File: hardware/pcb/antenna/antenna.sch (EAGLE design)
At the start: 25 parts, among them Q2 2N3819, T1 2N5089, X2 SMA-142-0701-801/806

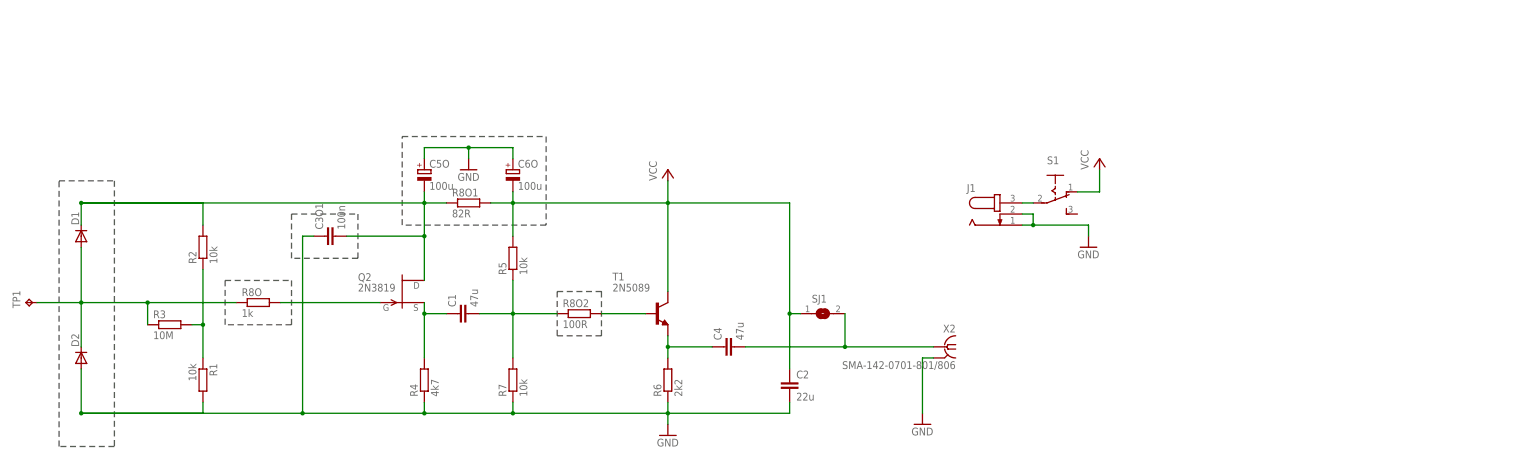
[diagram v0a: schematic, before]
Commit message: hw: added libs, modified receiver doc: added "proces dyplomowania" doc: added sample tex documents
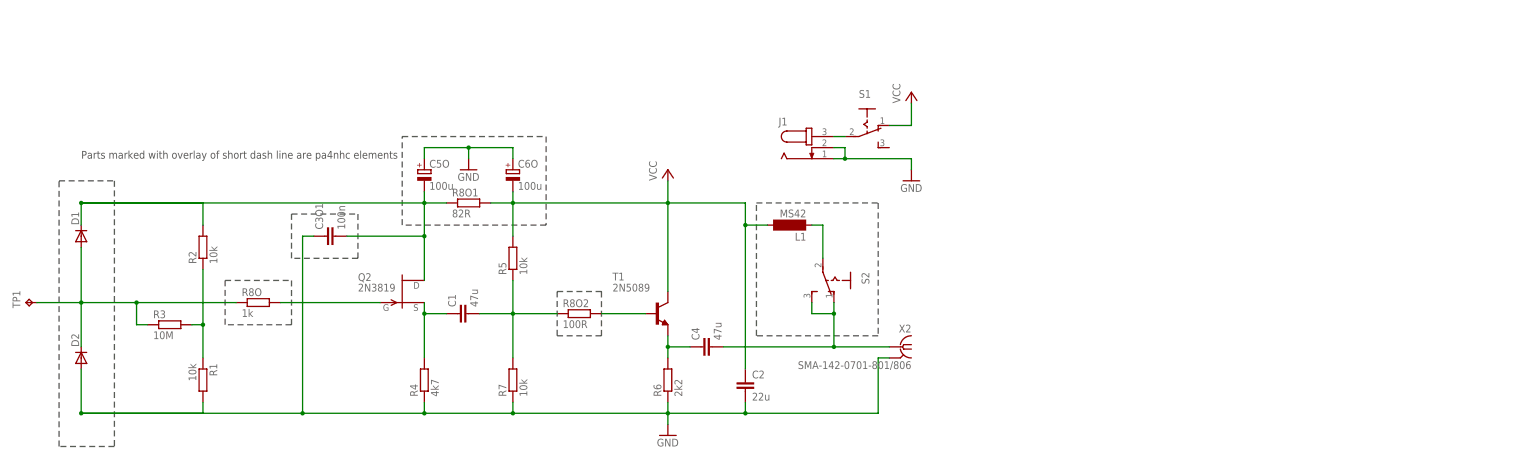
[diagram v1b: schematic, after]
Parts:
- removed SJ1: (no value), jumper:SJW
- added L1: MS42, inductor-neosid:MS42
- added S2: (no value), switch:255SB
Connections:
- new net N$6: L1.1, S2.P
- net N$7: now also S2.O, S2.S; no longer SJ1.2
- net VCC: now also L1.2; no longer SJ1.1
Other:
- note added: "Parts marked with overlay of short dash line are pa4nhc elements"
- moved on the sheet: C2, C4, J1, S1, X2

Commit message: hw: misc changes, added fuses to power supply units
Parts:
- added F1: 200mA, fuse:GSH15
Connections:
- new net N$12: F1.1, S1.O
- net VCC: now also F1.2; no longer S1.O
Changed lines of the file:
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@@
 <setting verticaltext="up"/>
 </settings>
-<grid distance="0.1" unitdist="inch" unit="inch" style="lines" multiple="1" display="yes" altdistance="0.01" altunitdist="inch" altunit="inch"/>
+<grid distance="0.1" unitdist="inch" unit="inch" style="lines" multiple="1" display="no" altdistance="0.01" altunitdist="inch" altunit="inch"/>
 <layers>
 <layer number="1" name="Top" color="4" fill="1" visible="no" active="no"/>
@@
 <part name="S2" library="switch" deviceset="255SB" device=""/>
 <part name="L1" library="inductor-neosid" deviceset="MS42" device=""/>
+<part name="F1" library="fuse" deviceset="GSH15" device="" value="200mA"/>
 </parts>
 <sheets>
@@
 <instance part="C6O" gate="G$1" x="71.12" y="63.5"/>
 <instance part="GND1" gate="1" x="106.68" y="2.54"/>
-<instance part="GND2" gate="1" x="162.56" y="60.96"/>
+<instance part="GND2" gate="1" x="172.72" y="60.96"/>
 <instance part="GND3" gate="1" x="60.96" y="63.5"/>
 <instance part="TP1" gate="G$1" x="-40.64" y="33.02" rot="R90"/>
@@
 <instance part="X2" gate="G1" x="160.02" y="22.86" rot="MR0"/>
 <instance part="J1" gate="G$1" x="139.7" y="68.58"/>
-<instance part="P+1" gate="VCC" x="162.56" y="81.28"/>
+<instance part="P+1" gate="VCC" x="172.72" y="83.82"/>
 <instance part="S1" gate="1" x="152.4" y="73.66" rot="R270"/>
 <instance part="P+2" gate="VCC" x="106.68" y="63.5"/>
@@
 <instance part="S2" gate="1" x="144.78" y="38.1" rot="R180"/>
 <instance part="L1" gate="G$1" x="134.62" y="50.8" rot="R180"/>
+<instance part="F1" gate="1" x="165.1" y="73.66"/>
 </instances>
 <busses>
@@
 <pinref part="GND2" gate="1" pin="GND"/>
 <pinref part="J1" gate="G$1" pin="1"/>
-<wire x1="162.56" y1="66.04" x2="162.56" y2="63.5" width="0.1524" layer="91"/>
+<wire x1="172.72" y1="66.04" x2="172.72" y2="63.5" width="0.1524" layer="91"/>
 <wire x1="144.78" y1="66.04" x2="147.32" y2="66.04" width="0.1524" layer="91"/>
 <pinref part="J1" gate="G$1" pin="2"/>
-<wire x1="147.32" y1="66.04" x2="162.56" y2="66.04" width="0.1524" layer="91"/>
+<wire x1="147.32" y1="66.04" x2="172.72" y2="66.04" width="0.1524" layer="91"/>
 <wire x1="144.78" y1="68.58" x2="147.32" y2="68.58" width="0.1524" layer="91"/>
 <wire x1="147.32" y1="68.58" x2="147.32" y2="66.04" width="0.1524" layer="91"/>
@@
 <net name="VCC" class="0">
 <segment>
-<pinref part="S1" gate="1" pin="O"/>
-<wire x1="157.48" y1="73.66" x2="162.56" y2="73.66" width="0.1524" layer="91"/>
-<wire x1="162.56" y1="73.66" x2="162.56" y2="78.74" width="0.1524" layer="91"/>
-<pinref part="P+1" gate="VCC" pin="VCC"/>
-</segment>
-<segment>
 <pinref part="R5" gate="G$1" pin="2"/>
 <wire x1="71.12" y1="55.88" x2="106.68" y2="55.88" width="0.1524" layer="91"/>
@@
 <junction x="124.46" y="50.8"/>
 </segment>
+<segment>
+<pinref part="F1" gate="1" pin="2"/>
+<wire x1="170.18" y1="73.66" x2="172.72" y2="73.66" width="0.1524" layer="91"/>
+<wire x1="172.72" y1="73.66" x2="172.72" y2="81.28" width="0.1524" layer="91"/>
+<pinref part="P+1" gate="VCC" pin="VCC"/>
+</segment>
 </net>
 <net name="N$4" class="0">
@@
 </segment>
 </net>
+<net name="N$12" class="0">
+<segment>
+<pinref part="S1" gate="1" pin="O"/>
+<pinref part="F1" gate="1" pin="1"/>
+<wire x1="160.02" y1="73.66" x2="157.48" y2="73.66" width="0.1524" layer="91"/>
+</segment>
+</net>

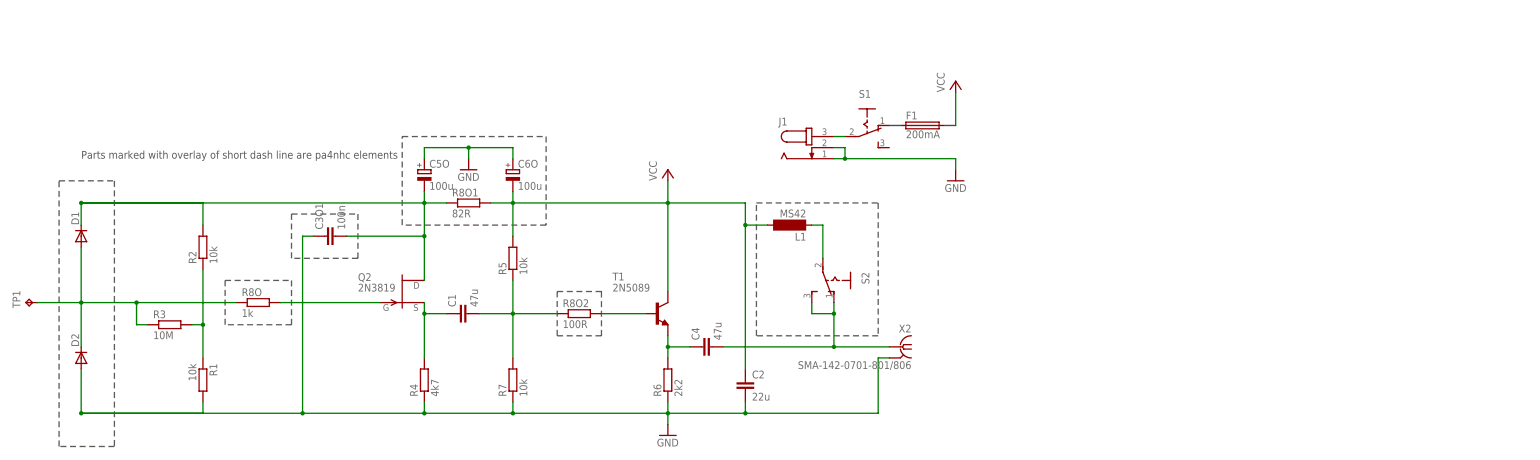
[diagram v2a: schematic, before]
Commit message: hw: added bibliography, fitler for 55MHz cutoff
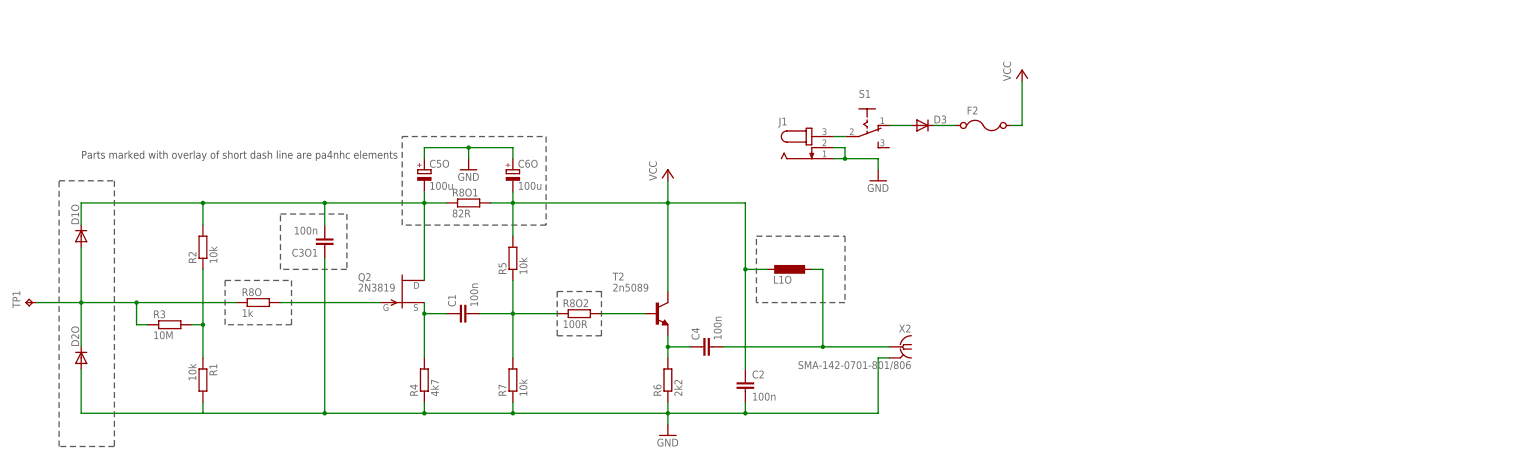
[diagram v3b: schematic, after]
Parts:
- removed D1, D2: (no value), diode:DIODE-SOD80C
- removed F1: 200mA, fuse:GSH15
- removed L1: MS42, inductor-neosid:MS42
- removed S2: (no value), switch:255SB
- removed T1: 2N5089, transistor:2N5089
- added D1O, D2O, D3: (no value), diode:DIODE-DO214AC
- added F2: (no value), lstolcman_thesis:0ZCG0150BF2C
- added L1O: (no value), rcl:L-EU0207/5V
- added T2: 2n5089, transistor:-NPN-SOT23-EBC
- C1, C4: value 47u -> 100n; MFR (none) -> C0805C104K5RACTU
- C2: value 22u -> 100n; MFR (none) -> C0805C104K5RACTU
- C3O1: MFR (none) -> C0805C104K5RACTU
- C5O, C6O: device rcl:CPOL-EUA/3216-18W -> rcl:CPOL-EUE2.5-7; MFR (none) -> 107CKS035M
- J1: MFR (none) -> 163-179PH-EX
- Q2: MFR (none) -> 2N3819 or 2N4859
- R1, R2, R5, R7: MFR (none) -> AS08J1002ET
- R3: MFR (none) -> SG73S2ATTD106J
- R4: MFR (none) -> SG73S2ATTD472J
- R6: device rcl:R-EU_M0805 -> rcl:R-EU_R2010; MFR (none) -> SG73P2ATTD222J
- R8O: MFR (none) -> AS08J1001ET
- R8O1: MFR (none) -> SG73S2ATTD820J
- R8O2: device rcl:R-EU_M0805 -> rcl:R-EU_M1206; MFR (none) -> AS08J1000ET
- S1: MFR (none) -> GF-123-3011
- TP1: MFR (none) -> LHL08TB100K
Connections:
- removed net N$7: C4.2, S2.O, S2.S, X2.1
- new net N$14: D3.C, F2.1
- net GND: now also D2O.A; no longer D2.A
- net N$1: now also D1O.A, D2O.C; no longer D1.A, D2.C
- net N$10: now also T2.B; no longer T1.B
- net N$12: now also D3.A; no longer F1.1
- net N$5: now also T2.E; no longer T1.E
- net N$6: now also C4.2, L1O.1, X2.1; no longer L1.1, S2.P
- net N$9: now also D1O.C; no longer D1.C
- net VCC: now also F2.2, L1O.2, T2.C; no longer F1.2, L1.2, T1.C
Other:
- moved on the sheet: C3O1

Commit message: hw: minor changes
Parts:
- added C3, C5, C6: 100n, rcl:C-EUC0805
- added L11: (no value), rcl:L-EU0207/5V
- added X1, X3: B35N57, con-coax:B35N57
- F2: MFR2 (none) -> 0ZCJ0020FF2E
- J1: MFR 163-179PH-EX -> FC68148; SUP (none) -> tme
- S1: MFR GF-123-3011 -> S1501; SUP (none) -> tme
- X2: value SMA-142-0701-801/806 -> B35N57; device con-coax:SMA-142-0701-801/806 -> con-coax:B35N57
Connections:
- new net N$13: D3.C, F2.2
- new net N$15: C6.1, X2.1
- new net N$7: C6.2, L11.2, X3.1
- net GND: now also C3.1, C5.1, X1.2, X3.2
- net N$12: now also C3.2, F2.1, L11.1; no longer D3.A, S1.O
- net N$14: now also C5.2, D3.A, S1.P; no longer D3.C, F2.1
- net N$6: now also X1.1; no longer X2.1
- net N$8: now also S1.O; no longer S1.P
- net VCC: no longer F2.2
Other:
- moved on the sheet: D3, F2, J1, S1

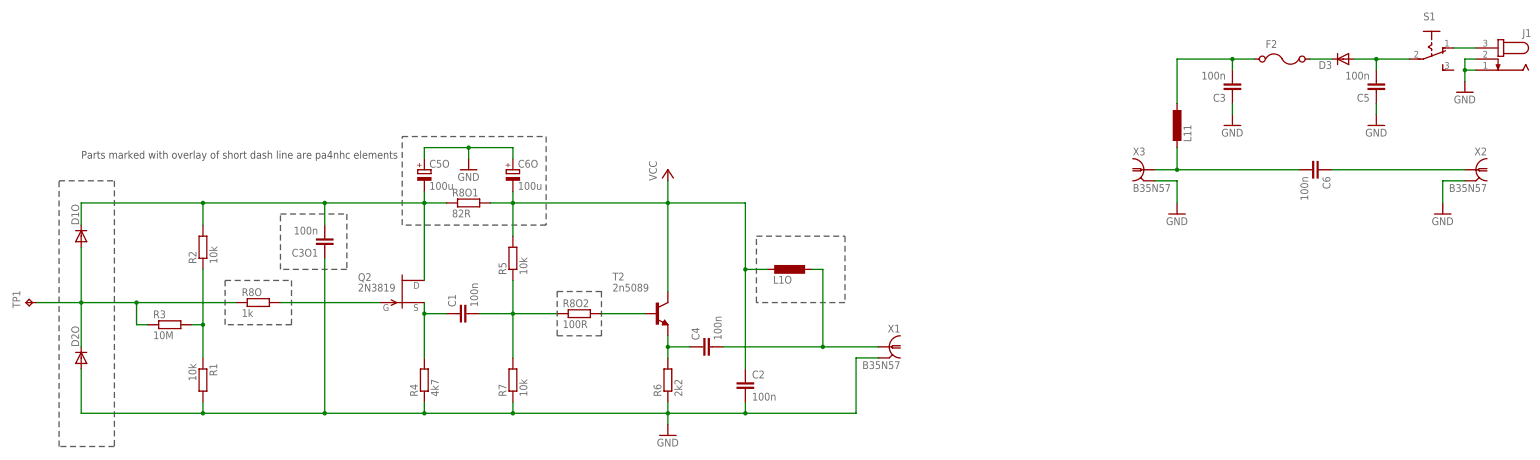
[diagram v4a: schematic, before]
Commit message: hw: bnc connector, misc changes
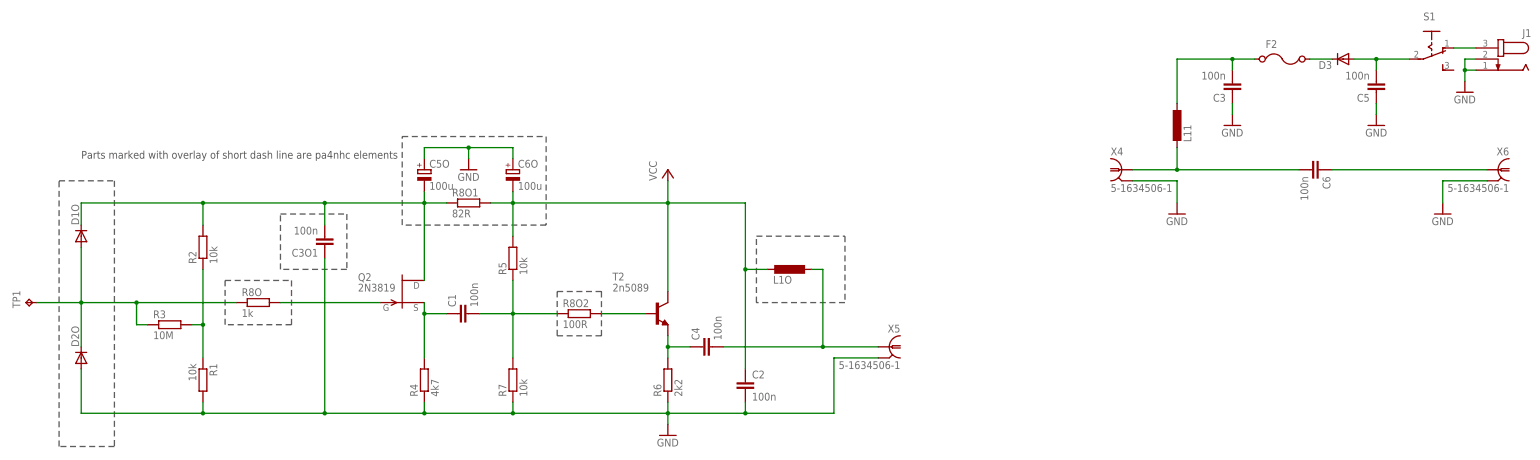
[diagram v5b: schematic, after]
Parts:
- removed X1, X2, X3: B35N57, con-coax:B35N57
- added X4, X5, X6: 5-1634506-1, lstolcman_thesis:5-1634506-1
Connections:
- net GND: now also X4.2, X5.2, X6.2; no longer X1.2, X2.2, X3.2
- net N$15: now also X6.1; no longer X2.1
- net N$6: now also X5.1; no longer X1.1
- net N$7: now also X4.1; no longer X3.1
